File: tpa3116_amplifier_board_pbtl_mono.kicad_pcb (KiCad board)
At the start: 2 copper layers, 59.7 x 50.8 mm, 47 parts, among them IC1 TPA3116D2QDADRQ1, J1 power_supply, J2 Conn_01x04, J3 power_supply, J4 output_right

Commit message: Изменил расположение переходных отверстий
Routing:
- net /SD_LR: track 35.4 -> 34.9 mm
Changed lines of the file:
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@@
   (segment (start 119.436 120.34) (end 118.872 120.904) (width 0.35) (layer "F.Cu") (net 5))
   (segment (start 119.0195 121.2645) (end 119.294 120.99) (width 0.35) (layer "F.Cu") (net 5))
-  (via (at 115.57 130.175) (size 0.8) (drill 0.4) (layers "F.Cu" "B.Cu") (free) (net 5))
   (via (at 122.533 113.665) (size 0.8) (drill 0.4) (layers "F.Cu" "B.Cu") (free) (net 5))
   (via (at 147.955 118.11) (size 0.8) (drill 0.4) (layers "F.Cu" "B.Cu") (free) (net 5))
   (via (at 125.73 125.095) (size 0.8) (drill 0.4) (layers "F.Cu" "B.Cu") (free) (net 5))
-  (via (at 112.395 125.73) (size 0.8) (drill 0.4) (layers "F.Cu" "B.Cu") (free) (net 5))
+  (via (at 110.49 123.825) (size 0.8) (drill 0.4) (layers "F.Cu" "B.Cu") (free) (net 5))
   (via (at 145.415 121.92) (size 0.8) (drill 0.4) (layers "F.Cu" "B.Cu") (free) (net 5))
   (via (at 142.875 129.54) (size 0.8) (drill 0.4) (layers "F.Cu" "B.Cu") (free) (net 5))
@@
   (via (at 147.955 107.95) (size 0.8) (drill 0.4) (layers "F.Cu" "B.Cu") (free) (net 5))
   (via (at 137.665 118.11) (size 0.8) (drill 0.4) (layers "F.Cu" "B.Cu") (free) (net 5))
-  (via (at 140.335 118.11) (size 0.8) (drill 0.4) (layers "F.Cu" "B.Cu") (free) (net 5))
   (via (at 123.19 114.935) (size 0.8) (drill 0.4) (layers "F.Cu" "B.Cu") (free) (net 5))
-  (via (at 145.415 134.62) (size 0.8) (drill 0.4) (layers "F.Cu" "B.Cu") (free) (net 5))
   (via (at 137.665 121.92) (size 0.8) (drill 0.4) (layers "F.Cu" "B.Cu") (free) (net 5))
+  (via (at 109.22 123.825) (size 0.8) (drill 0.4) (layers "F.Cu" "B.Cu") (free) (net 5))
   (via (at 122.533 109.855) (size 0.8) (drill 0.4) (layers "F.Cu" "B.Cu") (free) (net 5))
   (via (at 122.555 133.985) (size 0.8) (drill 0.4) (layers "F.Cu" "B.Cu") (free) (net 5))
   (via (at 145.415 132.08) (size 0.8) (drill 0.4) (layers "F.Cu" "B.Cu") (free) (net 5))
-  (via (at 109.855 117.475) (size 0.8) (drill 0.4) (layers "F.Cu" "B.Cu") (free) (net 5))
+  (via (at 110.49 117.475) (size 0.8) (drill 0.4) (layers "F.Cu" "B.Cu") (free) (net 5))
   (via (at 151.13 105.41) (size 0.8) (drill 0.4) (layers "F.Cu" "B.Cu") (free) (net 5))
   (via (at 125.73 122.555) (size 0.8) (drill 0.4) (layers "F.Cu" "B.Cu") (free) (net 5))
   (via (at 122.533 112.395) (size 0.8) (drill 0.4) (layers "F.Cu" "B.Cu") (free) (net 5))
-  (via (at 114.3 107.315) (size 0.8) (drill 0.4) (layers "F.Cu" "B.Cu") (free) (net 5))
+  (via (at 113.665 110.49) (size 0.8) (drill 0.4) (layers "F.Cu" "B.Cu") (free) (net 5))
   (via (at 123.825 107.315) (size 0.8) (drill 0.4) (layers "F.Cu" "B.Cu") (free) (net 5))
   (via (at 121.263 129.54) (size 0.8) (drill 0.4) (layers "F.Cu" "B.Cu") (free) (net 5))
@@
   (via (at 154.94 120.015) (size 0.8) (drill 0.4) (layers "F.Cu" "B.Cu") (free) (net 5))
   (via (at 156.845 120.015) (size 0.8) (drill 0.4) (layers "F.Cu" "B.Cu") (free) (net 5))
-  (via (at 111.125 117.475) (size 0.8) (drill 0.4) (layers "F.Cu" "B.Cu") (free) (net 5))
-  (via (at 112.395 130.175) (size 0.8) (drill 0.4) (layers "F.Cu" "B.Cu") (free) (net 5))
+  (via (at 111.76 117.475) (size 0.8) (drill 0.4) (layers "F.Cu" "B.Cu") (free) (net 5))
   (via (at 151.13 102.87) (size 0.8) (drill 0.4) (layers "F.Cu" "B.Cu") (free) (net 5))
   (via (at 124.46 116.205) (size 0.8) (drill 0.4) (layers "F.Cu" "B.Cu") (free) (net 5))
+  (via (at 147.955 120.015) (size 0.8) (drill 0.4) (layers "F.Cu" "B.Cu") (free) (net 5))
   (via (at 129.54 142.875) (size 0.8) (drill 0.4) (layers "F.Cu" "B.Cu") (free) (net 5))
   (via (at 134.62 142.875) (size 0.8) (drill 0.4) (layers "F.Cu" "B.Cu") (free) (net 5))
@@
   (via (at 124.46 125.095) (size 0.8) (drill 0.4) (layers "F.Cu" "B.Cu") (free) (net 5))
   (via (at 126.365 107.315) (size 0.8) (drill 0.4) (layers "F.Cu" "B.Cu") (free) (net 5))
-  (via (at 110.49 123.825) (size 0.8) (drill 0.4) (layers "F.Cu" "B.Cu") (free) (net 5))
+  (via (at 111.76 123.825) (size 0.8) (drill 0.4) (layers "F.Cu" "B.Cu") (free) (net 5))
+  (via (at 140.97 118.11) (size 0.8) (drill 0.4) (layers "F.Cu" "B.Cu") (free) (net 5))
   (via (at 156.21 137.16) (size 0.8) (drill 0.4) (layers "F.Cu" "B.Cu") (free) (net 5))
   (via (at 124.46 117.475) (size 0.8) (drill 0.4) (layers "F.Cu" "B.Cu") (free) (net 5))
@@
   (via (at 129.54 102.235) (size 0.8) (drill 0.4) (layers "F.Cu" "B.Cu") (free) (net 5))
   (via (at 122.533 111.125) (size 0.8) (drill 0.4) (layers "F.Cu" "B.Cu") (free) (net 5))
+  (via (at 145.415 120.015) (size 0.8) (drill 0.4) (layers "F.Cu" "B.Cu") (free) (net 5))
   (via (at 114.935 142.875) (size 0.8) (drill 0.4) (layers "F.Cu" "B.Cu") (free) (net 5))
   (via (at 156.845 123.825) (size 0.8) (drill 0.4) (layers "F.Cu" "B.Cu") (free) (net 5))
@@
   (via (at 121.263 128.27) (size 0.8) (drill 0.4) (layers "F.Cu" "B.Cu") (free) (net 5))
   (via (at 151.13 137.16) (size 0.8) (drill 0.4) (layers "F.Cu" "B.Cu") (free) (net 5))
+  (via (at 140.97 121.92) (size 0.8) (drill 0.4) (layers "F.Cu" "B.Cu") (free) (net 5))
   (via (at 151.13 139.7) (size 0.8) (drill 0.4) (layers "F.Cu" "B.Cu") (free) (net 5))
   (via (at 142.875 115.57) (size 0.8) (drill 0.4) (layers "F.Cu" "B.Cu") (free) (net 5))
@@
   (via (at 147.955 105.41) (size 0.8) (drill 0.4) (layers "F.Cu" "B.Cu") (free) (net 5))
   (via (at 123.19 123.825) (size 0.8) (drill 0.4) (layers "F.Cu" "B.Cu") (free) (net 5))
-  (via (at 115.57 125.73) (size 0.8) (drill 0.4) (layers "F.Cu" "B.Cu") (free) (net 5))
+  (via (at 116.205 129.54) (size 0.8) (drill 0.4) (layers "F.Cu" "B.Cu") (free) (net 5))
   (via (at 121.285 113.03) (size 0.8) (drill 0.4) (layers "F.Cu" "B.Cu") (free) (net 5))
   (via (at 119.38 102.235) (size 0.8) (drill 0.4) (layers "F.Cu" "B.Cu") (free) (net 5))
-  (via (at 108.585 117.475) (size 0.8) (drill 0.4) (layers "F.Cu" "B.Cu") (free) (net 5))
+  (via (at 109.22 117.475) (size 0.8) (drill 0.4) (layers "F.Cu" "B.Cu") (free) (net 5))
+  (via (at 116.205 127) (size 0.8) (drill 0.4) (layers "F.Cu" "B.Cu") (free) (net 5))
   (via (at 151.13 100.33) (size 0.8) (drill 0.4) (layers "F.Cu" "B.Cu") (free) (net 5))
   (via (at 151.13 134.62) (size 0.8) (drill 0.4) (layers "F.Cu" "B.Cu") (free) (net 5))
   (via (at 123.19 117.475) (size 0.8) (drill 0.4) (layers "F.Cu" "B.Cu") (free) (net 5))
-  (via (at 140.335 121.92) (size 0.8) (drill 0.4) (layers "F.Cu" "B.Cu") (free) (net 5))
   (via (at 114.3 97.155) (size 0.8) (drill 0.4) (layers "F.Cu" "B.Cu") (free) (net 5))
   (via (at 124.46 122.555) (size 0.8) (drill 0.4) (layers "F.Cu" "B.Cu") (free) (net 5))
   (via (at 125.73 123.825) (size 0.8) (drill 0.4) (layers "F.Cu" "B.Cu") (free) (net 5))
   (via (at 119.38 142.875) (size 0.8) (drill 0.4) (layers "F.Cu" "B.Cu") (free) (net 5))
-  (via (at 114.935 137.16) (size 0.8) (drill 0.4) (layers "F.Cu" "B.Cu") (free) (net 5))
+  (via (at 114.935 137.795) (size 0.8) (drill 0.4) (layers "F.Cu" "B.Cu") (free) (net 5))
   (via (at 145.415 107.95) (size 0.8) (drill 0.4) (layers "F.Cu" "B.Cu") (free) (net 5))
   (via (at 124.46 114.935) (size 0.8) (drill 0.4) (layers "F.Cu" "B.Cu") (free) (net 5))
@@
   (via (at 123.19 125.095) (size 0.8) (drill 0.4) (layers "F.Cu" "B.Cu") (free) (net 5))
   (via (at 122.533 126.365) (size 0.8) (drill 0.4) (layers "F.Cu" "B.Cu") (free) (net 5))
-  (via (at 145.415 105.41) (size 0.8) (drill 0.4) (layers "F.Cu" "B.Cu") (free) (net 5))
   (via (at 122.533 127.635) (size 0.8) (drill 0.4) (layers "F.Cu" "B.Cu") (free) (net 5))
   (via (at 121.285 110.49) (size 0.8) (drill 0.4) (layers "F.Cu" "B.Cu") (free) (net 5))
@@
   (via (at 116.205 111.125) (size 1) (drill 0.4) (layers "F.Cu" "B.Cu") (net 14))
   (via (at 116.205 112.395) (size 1) (drill 0.4) (layers "F.Cu" "B.Cu") (net 14))
-  (segment (start 107.95 120.015) (end 107.95 127) (width 0.35) (layer "B.Cu") (net 14))
   (segment (start 116.205 112.395) (end 110.49 112.395) (width 0.35) (layer "B.Cu") (net 14))
   (segment (start 116.205 111.125) (end 116.205 112.395) (width 0.6) (layer "B.Cu") (net 14))
   (segment (start 107.95 127) (end 108.07 127.12) (width 0.35) (layer "B.Cu") (net 14))
-  (segment (start 107.315 115.57) (end 107.315 119.38) (width 0.35) (layer "B.Cu") (net 14))
   (segment (start 108.07 127.12) (end 108.19 127.12) (width 0.35) (layer "B.Cu") (net 14))
-  (segment (start 110.49 112.395) (end 107.315 115.57) (width 0.35) (layer "B.Cu") (net 14))
-  (segment (start 107.315 119.38) (end 107.95 120.015) (width 0.35) (layer "B.Cu") (net 14))
+  (segment (start 110.49 112.395) (end 107.95 114.935) (width 0.35) (layer "B.Cu") (net 14))
+  (segment (start 107.95 114.935) (end 107.95 127) (width 0.35) (layer "B.Cu") (net 14))
   (segment (start 115.125 121.92) (end 115.125 123.825) (width 0.35) (layer "F.Cu") (net 15))
   (segment (start 120.672 119.69) (end 117.355 119.69) (width 0.35) (layer "F.Cu") (net 15))

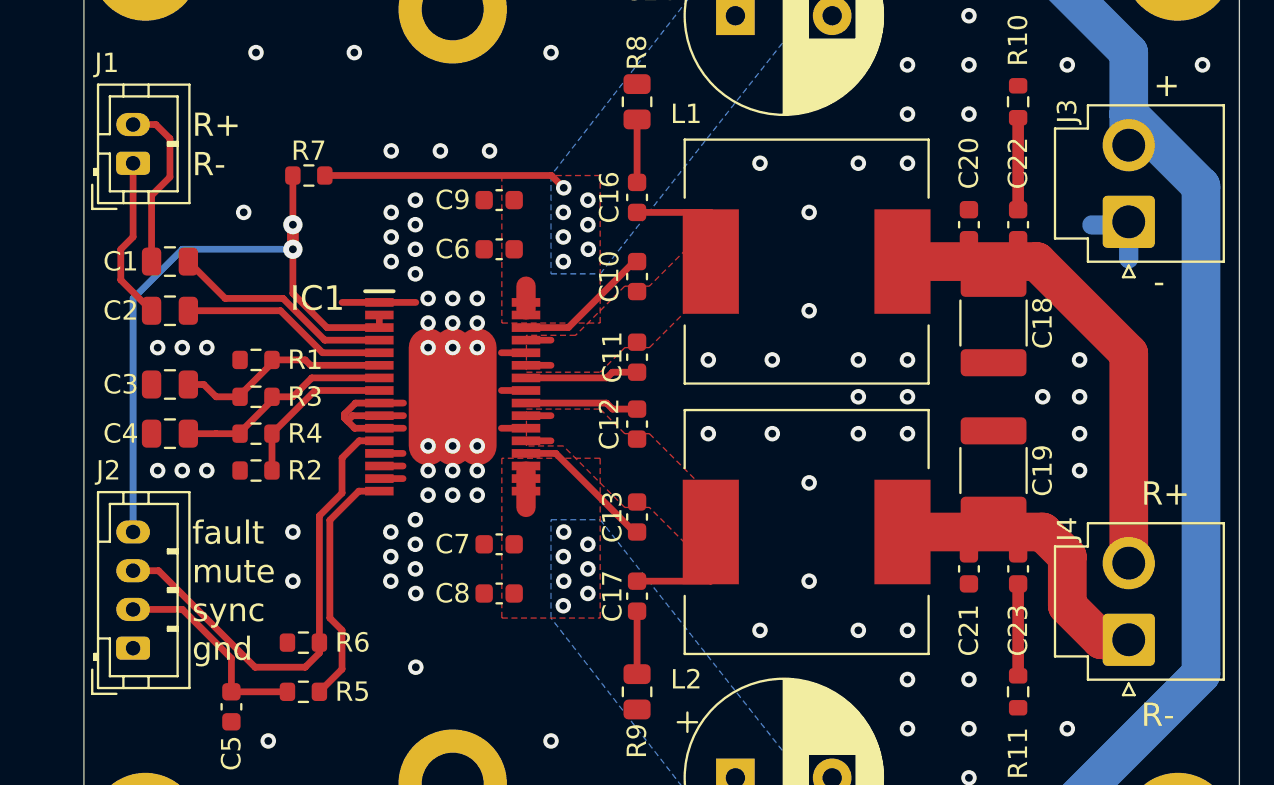
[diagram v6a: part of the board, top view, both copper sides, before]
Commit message: Увеличил размер отверстий под VH3.96
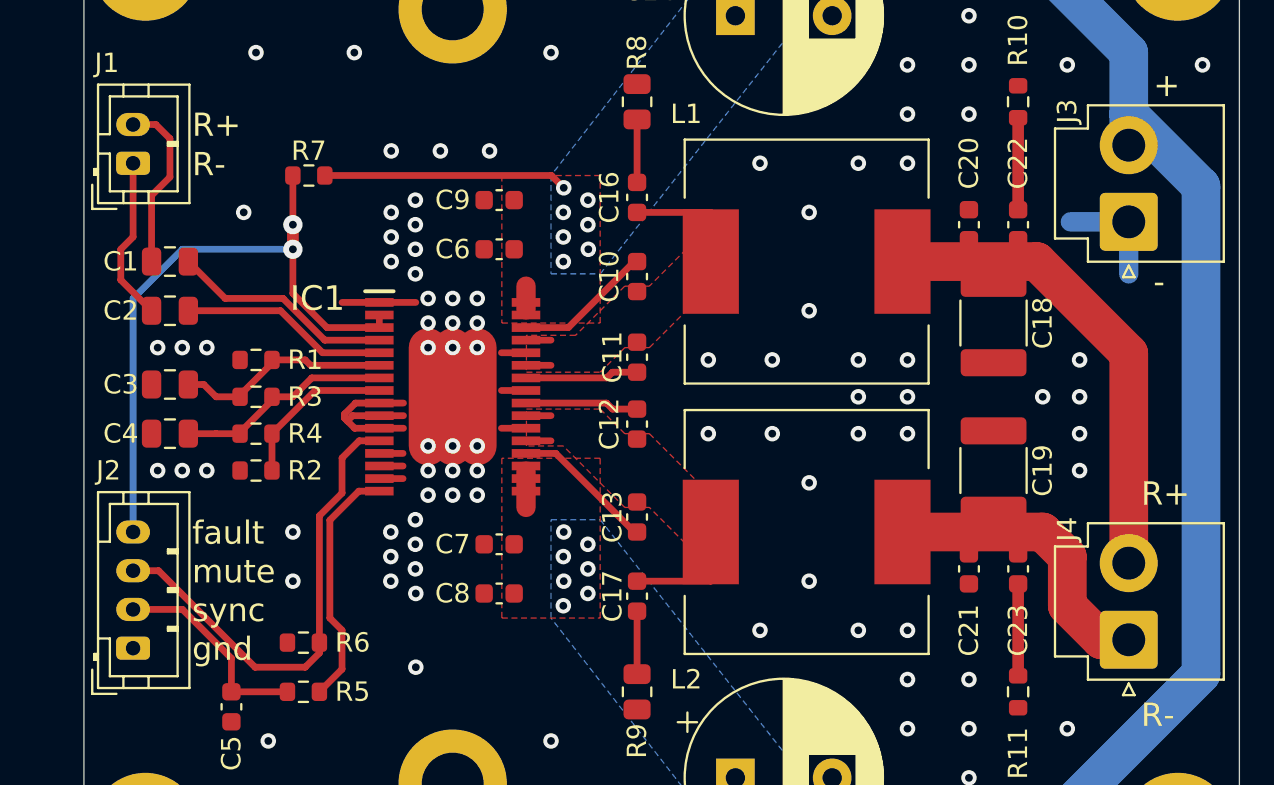
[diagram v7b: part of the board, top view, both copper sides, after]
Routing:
- net GND: track 40.6 -> 42.6 mm
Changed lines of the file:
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@@
     (fp_line (start 3.95 2.8) (end 3.95 -1.7)
       (stroke (width 0.1) (type solid)) (layer "F.Fab"))
-    (pad "1" thru_hole roundrect (at 0 0 90) (size 1.2 1.75) (drill 0.75) (layers "*.Cu" "*.Mask") (roundrect_rratio 0.208333)
+    (pad "1" thru_hole roundrect (at 0 0 90) (size 1.2 1.75) (drill 0.75) (layers "*.Cu" "*.Mask") (roundrect_rratio 0.2083333333)
       (net 3 "/R-") (pinfunction "Pin_1") (pintype "passive"))
     (pad "2" thru_hole oval (at 2 0 90) (size 1.2 1.75) (drill 0.75) (layers "*.Cu" "*.Mask")
@@
     (fp_line (start 5.91 4.8) (end 5.91 -2)
       (stroke (width 0.1) (type solid)) (layer "F.Fab"))
-    (pad "1" thru_hole roundrect (at 0 0 90) (size 2.7 2.7) (drill 1.7) (layers "*.Cu" "*.Mask") (roundrect_rratio 0.09259296296)
+    (pad "1" thru_hole roundrect (at 0 0 90) (size 3 3) (drill 1.7) (layers "*.Cu" "*.Mask") (roundrect_rratio 0.092593)
       (net 20 "Net-(J4-Pin_1)") (pinfunction "Pin_1") (pintype "passive"))
-    (pad "2" thru_hole circle (at 3.96 0 90) (size 2.7 2.7) (drill 1.7) (layers "*.Cu" "*.Mask")
+    (pad "2" thru_hole circle (at 3.96 0 90) (size 3 3) (drill 1.7) (layers "*.Cu" "*.Mask")
       (net 21 "Net-(J4-Pin_2)") (pinfunction "Pin_2") (pintype "passive"))
     (model "${KICAD6_3DMODEL_DIR}/Connector_JST.3dshapes/JST_VH_B2P-VH-B_1x02_P3.96mm_Vertical.wrl"
@@
     (fp_line (start 5.91 4.8) (end 5.91 -2)
       (stroke (width 0.1) (type solid)) (layer "F.Fab"))
-    (pad "1" thru_hole roundrect (at 0 0 90) (size 2.7 2.7) (drill 1.7) (layers "*.Cu" "*.Mask") (roundrect_rratio 0.09259296296)
+    (pad "1" thru_hole roundrect (at 0 0 90) (size 3 3) (drill 1.7) (layers "*.Cu" "*.Mask") (roundrect_rratio 0.092593)
       (net 5 "GND") (pinfunction "Pin_1") (pintype "passive"))
-    (pad "2" thru_hole circle (at 3.96 0 90) (size 2.7 2.7) (drill 1.7) (layers "*.Cu" "*.Mask")
+    (pad "2" thru_hole circle (at 3.96 0 90) (size 3 3) (drill 1.7) (layers "*.Cu" "*.Mask")
       (net 7 "VCC") (pinfunction "Pin_2") (pintype "passive"))
     (model "${KICAD6_3DMODEL_DIR}/Connector_JST.3dshapes/JST_VH_B2P-VH-B_1x02_P3.96mm_Vertical.wrl"
@@
     (fp_line (start 7.95 2.8) (end 7.95 -1.7)
       (stroke (width 0.1) (type solid)) (layer "F.Fab"))
-    (pad "1" thru_hole roundrect (at 0 0 90) (size 1.2 1.75) (drill 0.75) (layers "*.Cu" "*.Mask") (roundrect_rratio 0.208333)
+    (pad "1" thru_hole roundrect (at 0 0 90) (size 1.2 1.75) (drill 0.75) (layers "*.Cu" "*.Mask") (roundrect_rratio 0.2083333333)
       (net 5 "GND") (pinfunction "Pin_1") (pintype "passive"))
     (pad "2" thru_hole oval (at 2 0 90) (size 1.2 1.75) (drill 0.75) (layers "*.Cu" "*.Mask")
@@
   (via (at 163.195 102.87) (size 0.8) (drill 0.4) (layers "F.Cu" "B.Cu") (free) (net 5))
   (via (at 121.285 107.315) (size 0.8) (drill 0.4) (layers "F.Cu" "B.Cu") (free) (net 5))
-  (segment (start 159.385 111.1375) (end 157.48 111.1375) (width 1) (layer "B.Cu") (net 5))
-  (segment (start 159.385 111.1375) (end 159.385 112.8825) (width 1) (layer "B.Cu") (net 5))
+  (segment (start 159.385 110.9775) (end 156.37 110.9775) (width 1) (layer "B.Cu") (net 5))
+  (segment (start 159.385 113.665) (end 159.385 110.9775) (width 1) (layer "B.Cu") (net 5))
   (segment (start 116.205 120.015) (end 117.18 119.04) (width 0.35) (layer "F.Cu") (net 6))
   (segment (start 113.643 121.92) (end 112.235 121.92) (width 0.35) (layer "F.Cu") (net 6))
